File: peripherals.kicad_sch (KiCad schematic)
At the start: 67 parts, among them J15 Molex_PicoBlade_1x4_0533980471, J16 JST_SH_1x4_SM04B-SRSS-TB-LF-SN, J17 JST_SH_1x4_SM04B-SRSS-TB-LF-SN, Q1 DMG1012T-7, Q13 DMG1012T-7, Q14 DMG1012T-7, U14 SLB9673AU20FW2610XTMA1, U16 TPD4E05U06QDQARQ1, U51 NTS0102_XSON, U53 AP22615A_TSOT26, U54 AT24CS01_SOT23, U55 AP22615A_TSOT26, U67 TPD4E05U06QDQARQ1, U68 TPD4E05U06QDQARQ1, U71 PCAL6408A_VQFN

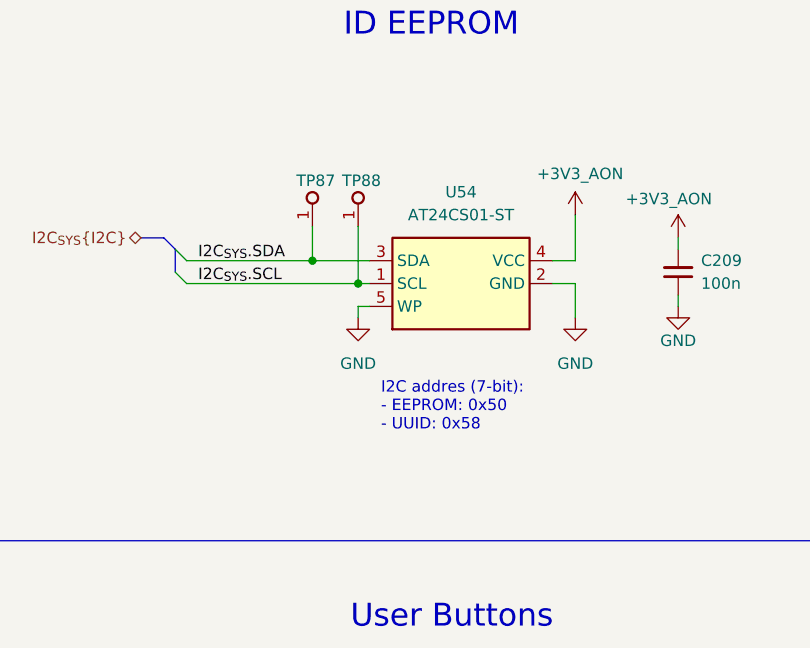
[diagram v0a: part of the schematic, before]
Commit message: [#85702] FMC schematic update
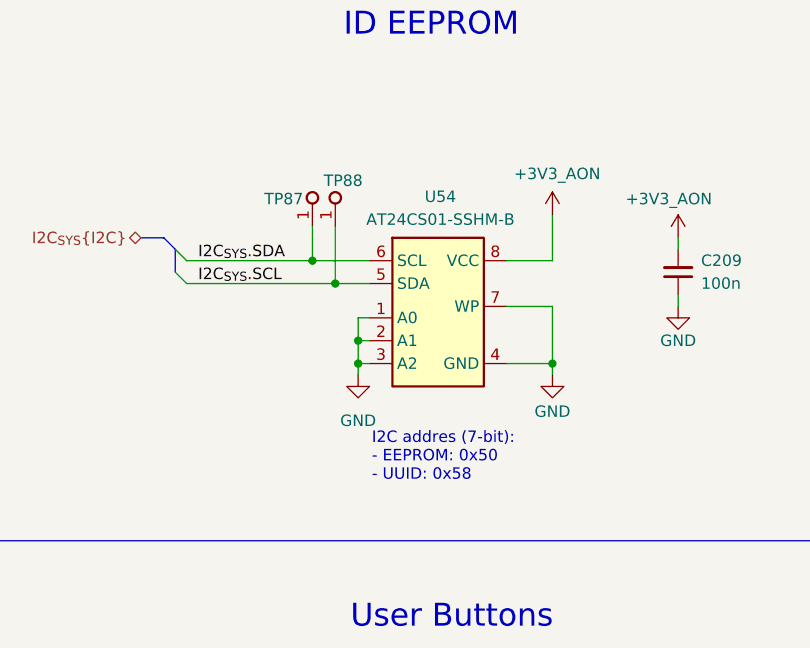
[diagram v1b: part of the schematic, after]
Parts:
- U54: value AT24CS01_SOT23 -> AT24CS01_SOIC8; footprint antmicro-footprints:SOT-23-5 -> antmicro-footprints:SOIC-8-1EP_3.9x4.9x1.75mm_P1.27mm; symbol antmicroMemory:AT24CS01_SOT23 -> antmicroMemory:AT24CS01_SOIC8; MPN AT24CS01-ST -> AT24CS01-SSHM-B; Manufacturer Atmel -> Microchip Technology
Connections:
- net +3V3_AON: now also U54.8 (VCC); no longer U54.4 (VCC)
- net GND: now also U54.1 (A0), U54.3 (A2), U54.4 (GND), U54.7 (WP); no longer U54.5 (WP)
- net I2C_{SYS}.SCL: now also U54.5 (SDA); no longer U54.1 (SCL)
- net I2C_{SYS}.SDA: now also U54.6 (SCL); no longer U54.3 (SDA)
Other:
- moved on the sheet: TP88

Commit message: Update naming on schematic sheets and PCB, update release date
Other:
- title: Jetson AGX Thor Baseboard -> Antmicro Baseboard for Jetson AGX Thor
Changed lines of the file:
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@@
 	(paper "A3")
 	(title_block
-		(title "Jetson AGX Thor Baseboard")
-		(date "2025-11-03")
+		(title "Antmicro Baseboard for Jetson AGX Thor")
+		(date "2026-02-17")
 		(rev "1.1.0")
 		(company "Antmicro Ltd")

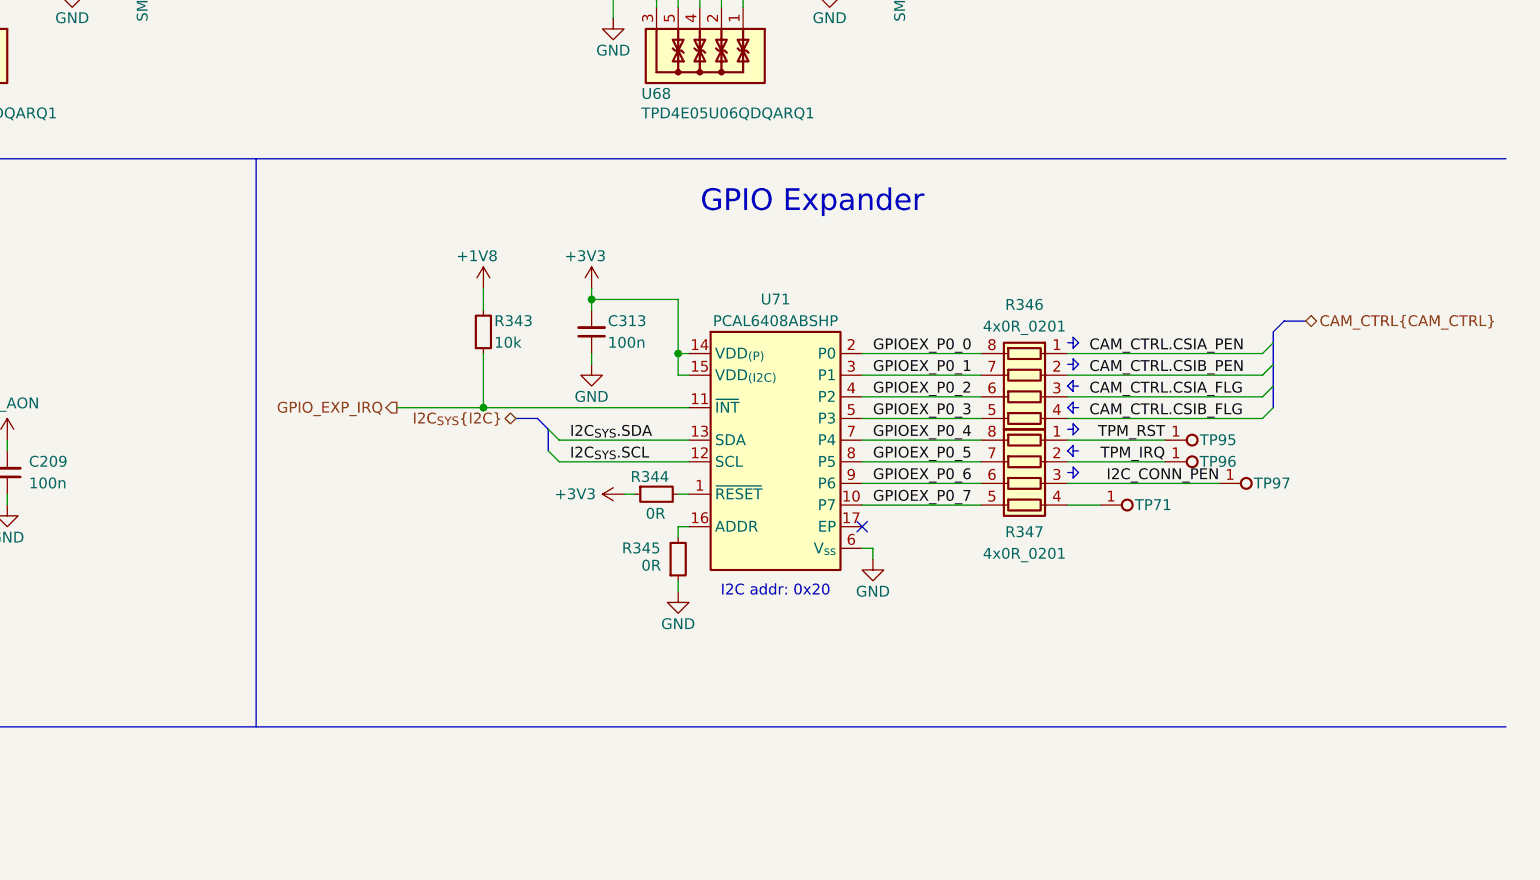
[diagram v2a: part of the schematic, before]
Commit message: [#88665] All Resistors array replaced by standalone resistors
Task done as described in #88665
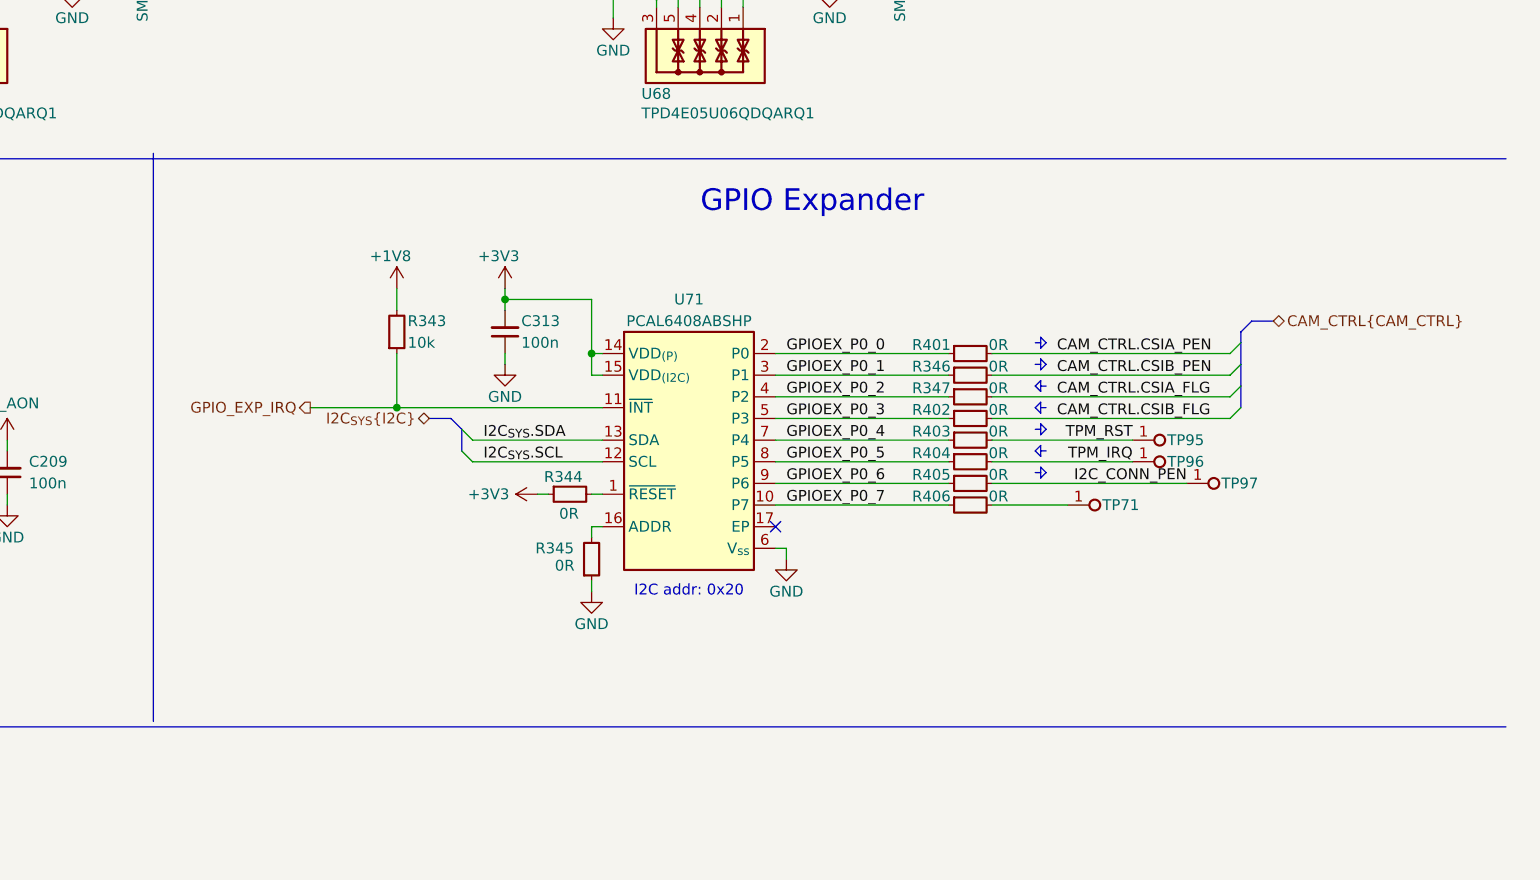
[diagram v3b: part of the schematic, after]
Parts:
- removed R346, R347: R_4x0R_0201_array, antmicro-footprints:R_Array_4x0201_Panasonic_EXB18V, symbol antmicroResistorNetworksArrays:R_4x0R_0201_array
- added R346, R347, R401, R402, R403, R404, R405, R406: R_0R_0402, antmicro-footprints:R_0402_1005Metric, symbol antmicroResistors0402:R_0R_0402
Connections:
- net CAM_CTRL.CSIA_FLG: now also R347.2
- net CAM_CTRL.CSIA_PEN: now also R401.2
- net CAM_CTRL.CSIB_FLG: now also R402.2
- net CAM_CTRL.CSIB_PEN: now also R346.2
- net GPIOEX_P0_0: now also R401.1
- net GPIOEX_P0_1: now also R346.1
- net GPIOEX_P0_2: now also R347.1
- net GPIOEX_P0_3: now also R402.1
- net GPIOEX_P0_4: now also R403.1
- net GPIOEX_P0_5: now also R404.1
- net GPIOEX_P0_6: now also R405.1
- net GPIOEX_P0_7: now also R406.1
- net I2C_CONN_PEN: now also R405.2
- net TPM_IRQ: now also R404.2
- net TPM_RST: now also R403.2
- net at TP71.1: now also R406.2
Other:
- moved on the sheet: C313, R343, R344, R345, TP71, TP95, TP96, TP97, U71

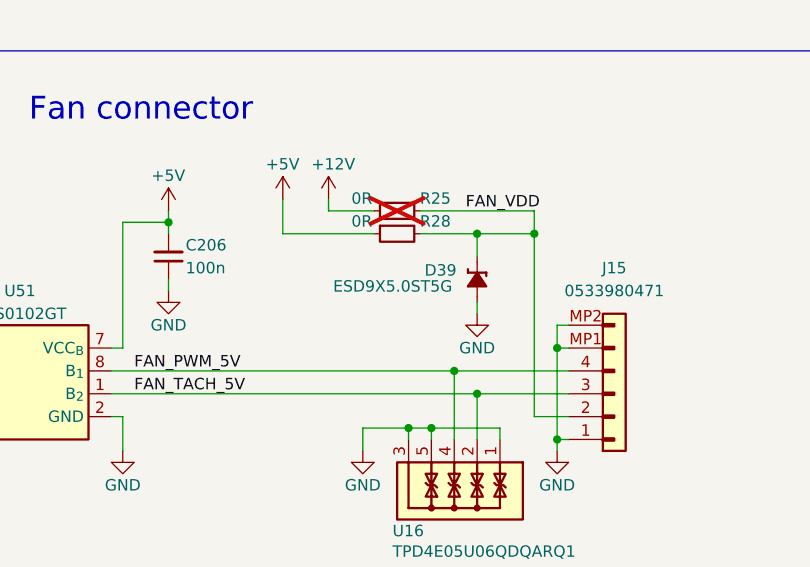
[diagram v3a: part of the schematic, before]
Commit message: [#88664] ESD9X5.0ST5G diodes replaced by PESD5Z5_0F, added TVS on Fan 12V
ESD9X5.0ST5G -> PESD5Z5_0F, changes done on schematics and PCB editor,
added TVS for fan 12V
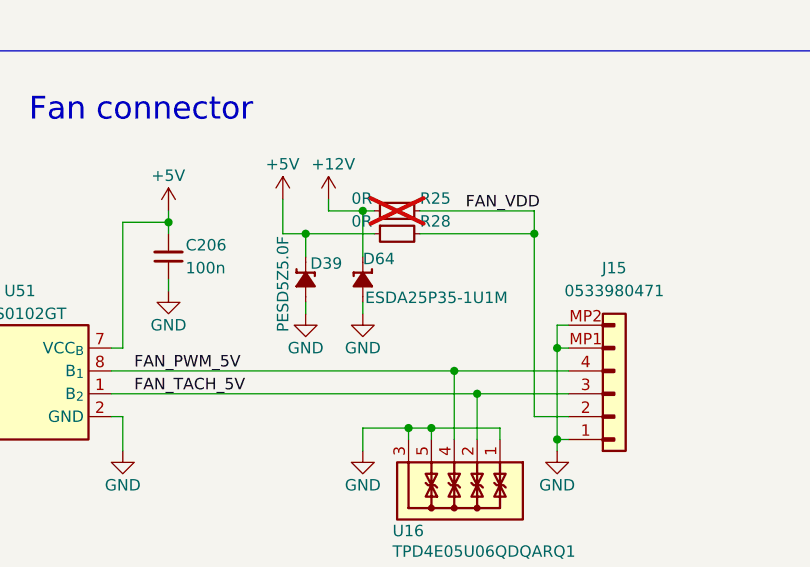
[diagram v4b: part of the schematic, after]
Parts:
- added D64: ESDA25P35-1U1M, antmicro-footprints:QFN-2L_1.6x1x0.55mm, symbol antmicroTVSDiodes:ESDA25P35-1U1M
- D39: value ESD9X5.0ST5G -> PESD5Z5.0F; footprint antmicro-footprints:SOD-923 -> antmicro-footprints:SOD-523; symbol antmicroTVSDiodes:ESD9X5.0ST5G -> antmicroTVSDiodes:PESD5Z5_0F; MPN ESD9X5.0ST5G -> PESD5Z5.0F; Manufacturer ON Semiconductor -> Nexperia
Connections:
- net +12V: now also D64.1 (C)
- net +5V: now also D39.1 (C)
- net FAN_VDD: no longer D39.1 (C)
- net GND: now also D64.2 (A)
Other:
- moved on the sheet: D39

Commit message: [#90793] Correct symbol and footprint properties, sync sch to PCB, change J21 to top entry connector
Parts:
- Q1, Q13, Q14: now in the parts list
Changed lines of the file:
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@@
 		(unit 1)
 		(exclude_from_sim no)
-		(in_bom no)
+		(in_bom yes)
 		(on_board yes)
 		(dnp no)
@@
 		(unit 1)
 		(exclude_from_sim no)
-		(in_bom no)
+		(in_bom yes)
 		(on_board yes)
 		(dnp no)
@@
 		(unit 1)
 		(exclude_from_sim no)
-		(in_bom no)
+		(in_bom yes)
 		(on_board yes)
 		(dnp no)
